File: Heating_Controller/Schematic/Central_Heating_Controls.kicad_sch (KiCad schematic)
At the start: 22 parts, among them J1 Mains In, J2 Output to Zone Valves, J3 Logic Control Input, J4 Thermostat Input, J5 Boiler Demand, J6 Valve(s) Open, K1 Zone 1, K2 Zone 2, K3 Zone 3, K4 Zone 4, K5 Boiler Demand, SW1 Zone 1 Mode, SW2 Zone 2 Mode, SW3 Zone 3 Mode, SW4 Zone 4 (HW) Mode, SW5 SW_SPST, SW6 Cylinder Stat

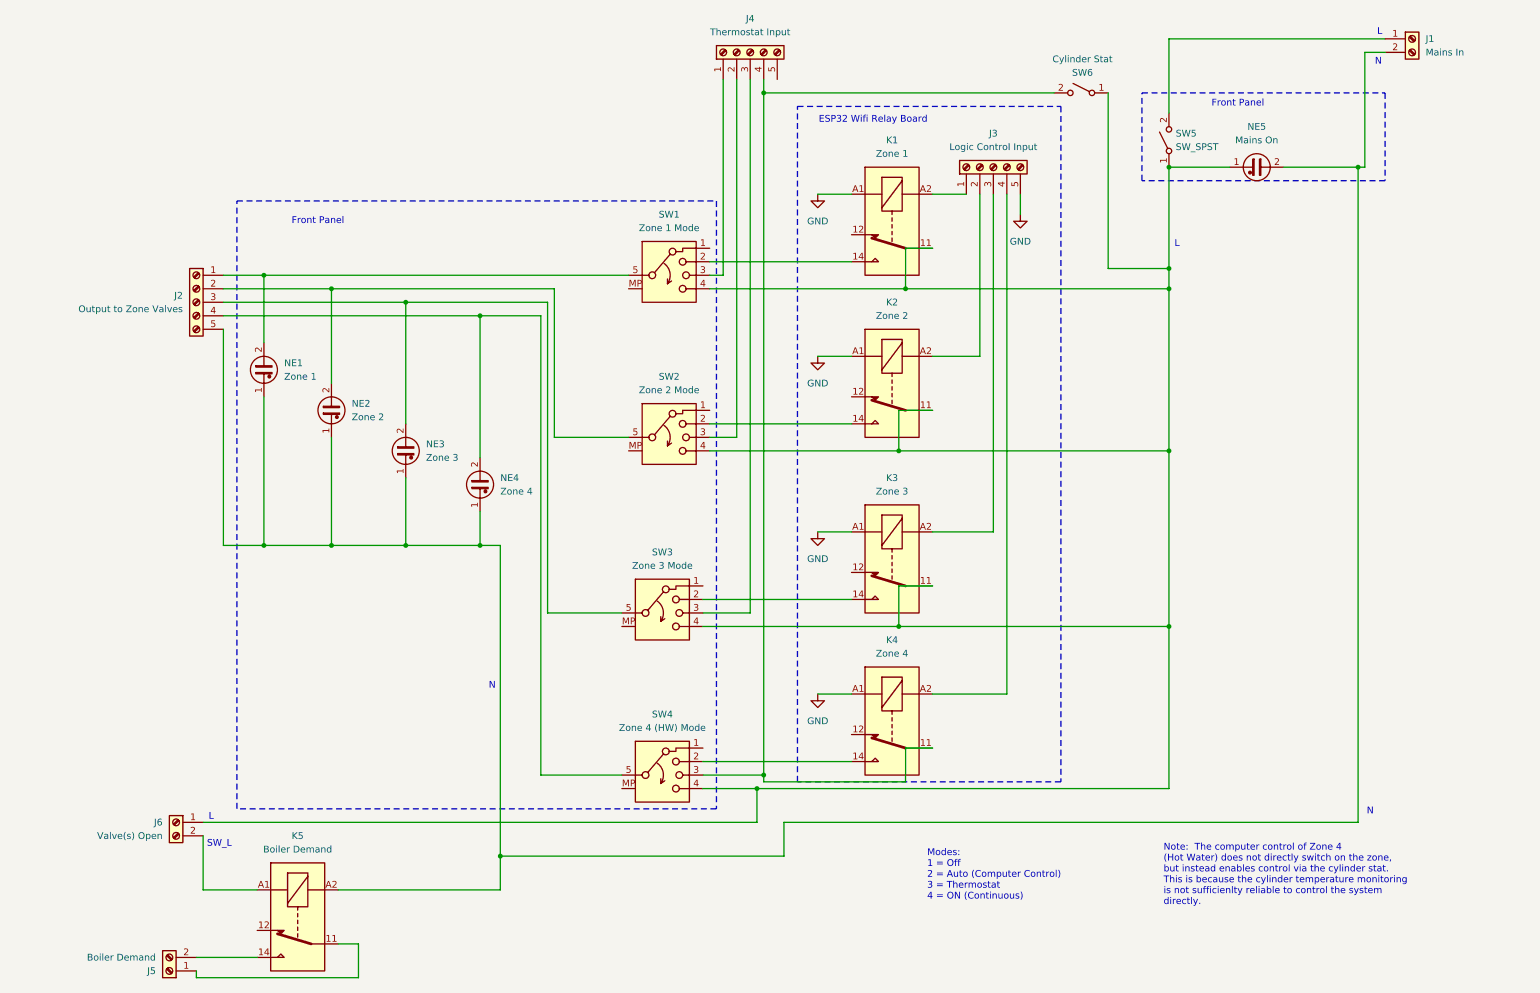
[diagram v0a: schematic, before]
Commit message: Re-ordered components on schematic to make it simpler to read
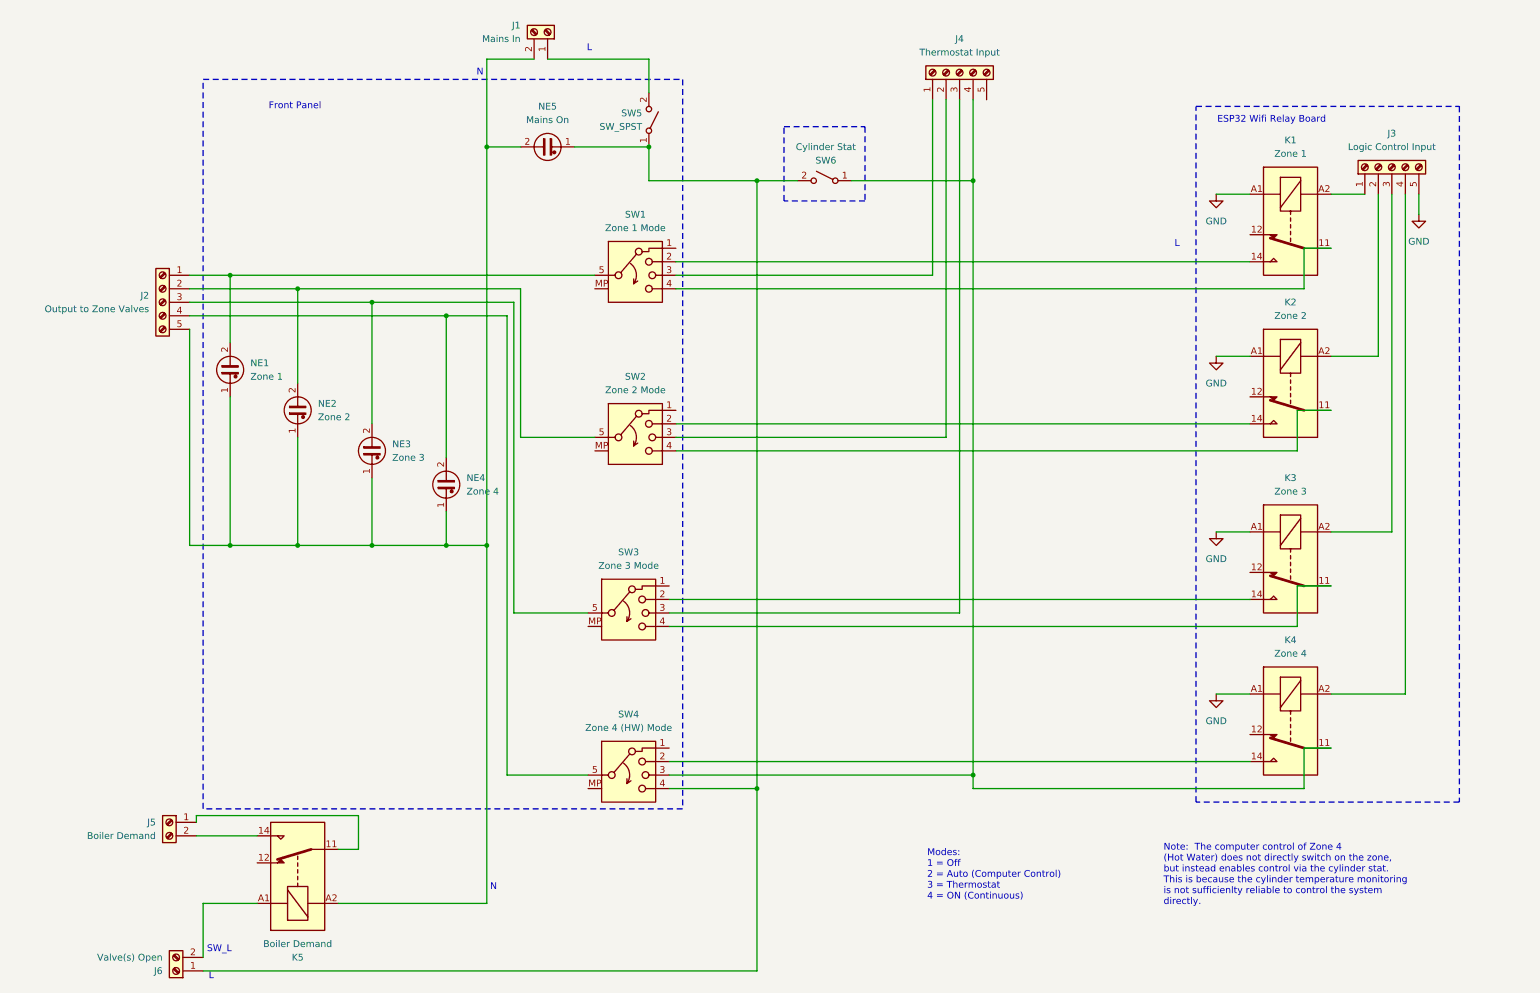
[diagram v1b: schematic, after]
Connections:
- net at J4.4 (Pin_4), K4.11, SW4.3: now also SW6.1 (A); no longer SW6.2 (B)
- new net: K2.11, SW2.4
- new net: K3.11, SW3.4
- new net: J6.1 (Pin_1), NE5.1, SW4.4, SW5.1 (A), SW6.2 (B)
- new net: K1.11, SW1.4
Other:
- moved on the sheet: J1, J2, J3, J4, J5, J6, K1, K2, K3, K4, K5, NE1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

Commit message: Added extra sheets to schematic for thermostat relay panel and valves junction box.
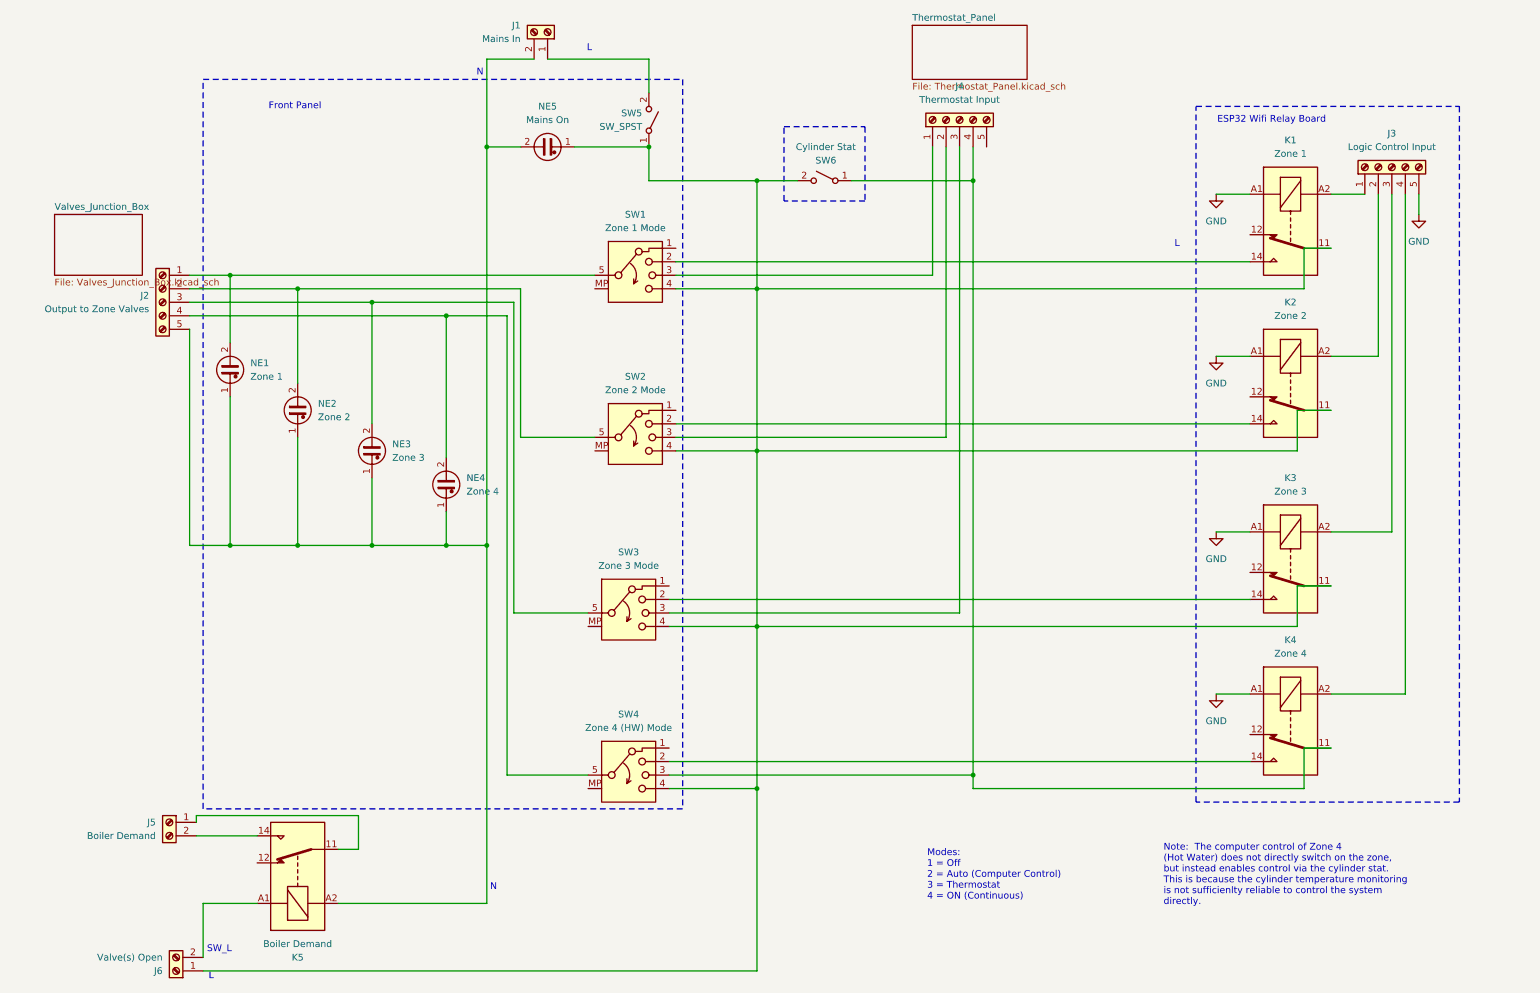
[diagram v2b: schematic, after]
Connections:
- net at K2.11, SW2.4: now also J6.1 (Pin_1), K1.11, K3.11, NE5.1, SW1.4, SW3.4, SW4.4, SW5.1 (A), SW6.2 (B)
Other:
- added sheet Thermostat_Panel (Thermostat_Panel.kicad_sch)
- added sheet Valves_Junction_Box (Valves_Junction_Box.kicad_sch)
- moved on the sheet: J4
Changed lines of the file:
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@@
 	(title_block
 		(title "Boiler Control Panel 1")
-		(date "05/12/2024")
-		(rev "2")
+		(date "11/12/2024")
+		(rev "3")
 	)
 	(junction
@@
 	)
 	(junction
+		(at 148.59 127)
+		(diameter 0)
+		(color 0 0 0 0)
+	)
+	(junction
 		(at 148.59 43.18)
 		(diameter 0)
@@
 	)
 	(junction
+		(at 148.59 63.5)
+		(diameter 0)
+		(color 0 0 0 0)
+	)
+	(junction
 		(at 76.2 111.76)
 		(diameter 0)
 		(color 0 0 0 0)
 	)
+	(junction
+		(at 148.59 93.98)
+		(diameter 0)
+		(color 0 0 0 0)
+	)
 	(wire
 		(pts
@@
 	(wire
 		(pts
-			(xy 133.35 63.5) (xy 251.46 63.5)
+			(xy 133.35 63.5) (xy 148.59 63.5)
 		)
 		(stroke
@@
 	(wire
 		(pts
-			(xy 148.59 157.48) (xy 148.59 43.18)
+			(xy 148.59 157.48) (xy 148.59 127)
 		)
 		(stroke
@@
 	(wire
 		(pts
-			(xy 132.08 127) (xy 250.19 127)
+			(xy 132.08 127) (xy 148.59 127)
 		)
 		(stroke
@@
 	(wire
 		(pts
-			(xy 189.23 27.94) (xy 189.23 43.18)
-		)
-		(stroke
-			(width 0)
-			(type default)
-		)
-	)
-	(wire
-		(pts
-			(xy 186.69 27.94) (xy 186.69 124.46)
+			(xy 189.23 36.83) (xy 189.23 43.18)
+		)
+		(stroke
+			(width 0)
+			(type default)
+		)
+	)
+	(wire
+		(pts
+			(xy 186.69 36.83) (xy 186.69 124.46)
 		)
 		(stroke
@@
 	(wire
 		(pts
+			(xy 148.59 127) (xy 250.19 127)
+		)
+		(stroke
+			(width 0)
+			(type default)
+		)
+	)
+	(wire
+		(pts
 			(xy 90.17 105.41) (xy 90.17 111.76)
 		)
@@
 	(wire
 		(pts
+			(xy 148.59 93.98) (xy 148.59 63.5)
+		)
+		(stroke
+			(width 0)
+			(type default)
+		)
+	)
+	(wire
+		(pts
 			(xy 97.79 179.07) (xy 69.85 179.07)
 		)
@@
 	(wire
 		(pts
+			(xy 148.59 127) (xy 148.59 93.98)
+		)
+		(stroke
+			(width 0)
+			(type default)
+		)
+	)
+	(wire
+		(pts
+			(xy 148.59 63.5) (xy 148.59 43.18)
+		)
+		(stroke
+			(width 0)
+			(type default)
+		)
+	)
+	(wire
+		(pts
 			(xy 128.27 43.18) (xy 128.27 36.83)
 		)
@@
 	(wire
 		(pts
-			(xy 184.15 27.94) (xy 184.15 91.44)
+			(xy 184.15 36.83) (xy 184.15 91.44)
 		)
 		(stroke
@@
 	(wire
 		(pts
-			(xy 181.61 27.94) (xy 181.61 60.96)
+			(xy 148.59 93.98) (xy 250.19 93.98)
+		)
+		(stroke
+			(width 0)
+			(type default)
+		)
+	)
+	(wire
+		(pts
+			(xy 181.61 36.83) (xy 181.61 60.96)
 		)
 		(stroke
@@
 	(wire
 		(pts
-			(xy 133.35 93.98) (xy 250.19 93.98)
+			(xy 148.59 63.5) (xy 251.46 63.5)
+		)
+		(stroke
+			(width 0)
+			(type default)
+		)
+	)
+	(wire
+		(pts
+			(xy 133.35 93.98) (xy 148.59 93.98)
 		)
 		(stroke
@@
 	(symbol
 		(lib_id "Connector:Screw_Terminal_01x05")
-		(at 186.69 22.86 90)
+		(at 186.69 31.75 90)
 		(unit 1)
 		(exclude_from_sim no)
@@
 		(fields_autoplaced yes)
 		(property "Reference" "J4"
-			(at 186.69 16.51 90)
+			(at 186.69 25.4 90)
 			(effects
 				(font
@@
 		)
 		(property "Value" "Thermostat Input"
-			(at 186.69 19.05 90)
+			(at 186.69 27.94 90)
 			(effects
 				(font
@@
 		)
 		(property "Footprint" ""
-			(at 186.69 22.86 0)
+			(at 186.69 31.75 0)
 			(effects
 				(font
@@
 		)
 		(property "Datasheet" "~"
-			(at 186.69 22.86 0)
+			(at 186.69 31.75 0)
 			(effects
 				(font
@@
 		)
 		(property "Description" "Generic screw terminal, single row, 01x05, script generated (kicad-library-utils/schlib/autogen/connector/)"
-			(at 186.69 22.86 0)
+			(at 186.69 31.75 0)
 			(effects
 				(font
@@
 				)
 			)
+		)
+	)
+	(sheet
+		(at 16.51 49.53)
+		(size 16.51 11.43)
+		(fields_autoplaced yes)
+		(stroke
+			(width 0.1524)
+			(type solid)
+		)
+		(fill
+			(color 0 0 0 0.0000)
+		)
+		(property "Sheetname" "Valves_Junction_Box"
+			(at 16.51 48.8184 0)
+			(effects
+				(font
+					(size 1.27 1.27)
+				)
+				(justify left bottom)
+			)
+		)
+		(property "Sheetfile" "Valves_Junction_Box.kicad_sch"
+			(at 16.51 61.5446 0)
+			(effects
+				(font
+					(size 1.27 1.27)
+				)
+				(justify left top)
+			)
+		)
+		(instances
+			(project "Central_Heating_Controls"
+				(path "/cd955688-bdae-4275-b855-3d8eea9a4e1c"
+					(page "3")
+				)
+			)
+		)
+	)
+	(sheet
+		(at 177.8 13.97)
+		(size 21.59 10.16)
+		(fields_autoplaced yes)
+		(stroke
+			(width 0.1524)
+			(type solid)
+		)
+		(fill
+			(color 0 0 0 0.0000)
+		)
+		(property "Sheetname" "Thermostat_Panel"
+			(at 177.8 13.2584 0)
+			(effects
+				(font
+					(size 1.27 1.27)
+				)
+				(justify left bottom)
+			)
+		)
+		(property "Sheetfile" "Thermostat_Panel.kicad_sch"
+			(at 177.8 24.7146 0)
+			(effects
+				(font
+					(size 1.27 1.27)
+				)
+				(justify left top)
+			)
+		)
+		(instances
+			(project "Central_Heating_Controls"
+				(path "/cd955688-bdae-4275-b855-3d8eea9a4e1c"
+					(page "2")
+				)
+			)

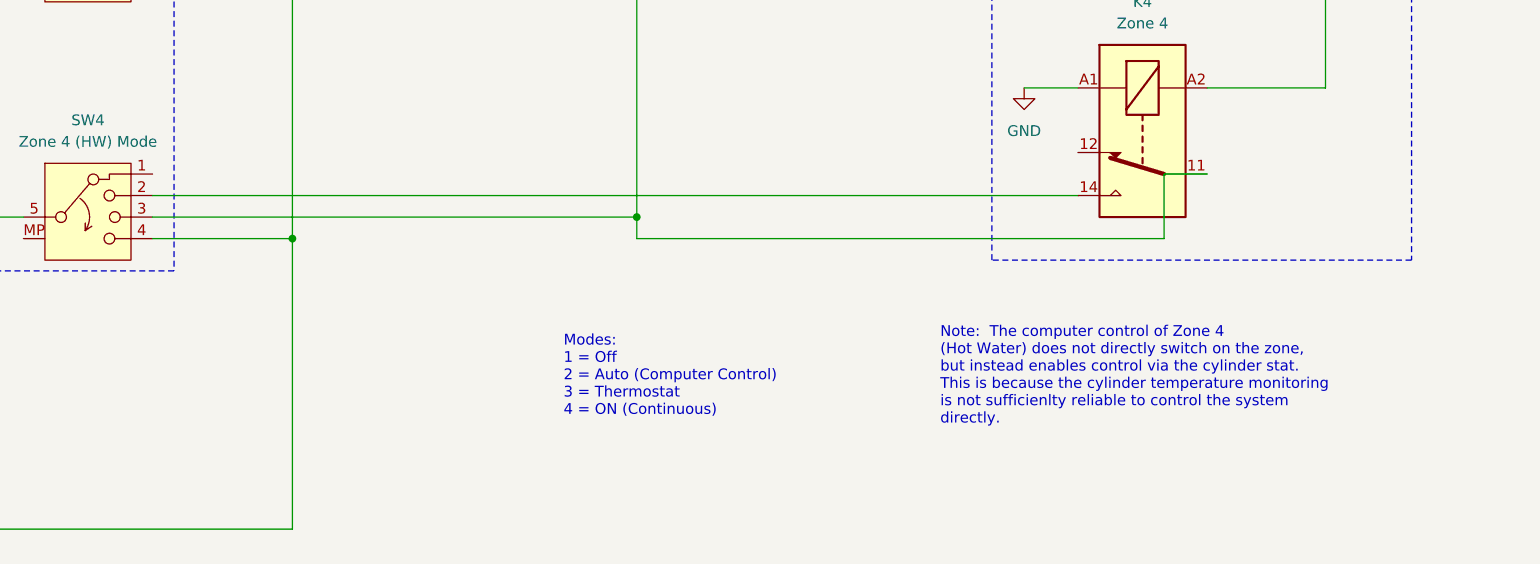
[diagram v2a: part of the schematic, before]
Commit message: Updated schematic to show DHW relay normally de-energised
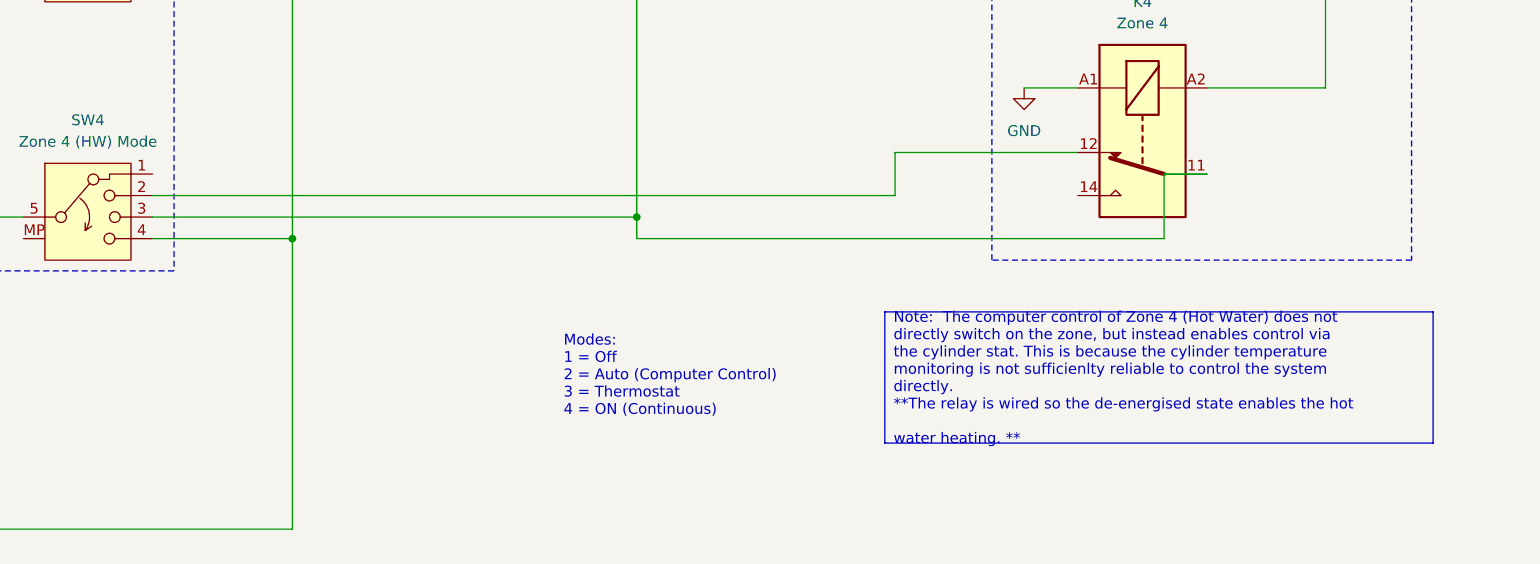
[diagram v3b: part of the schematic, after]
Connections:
- net at SW4.2: now also K4.12; no longer K4.14
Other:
- note removed: "Note: The computer control of Zone 4 (Hot Water) does not directly switch on the zone, but instead enables control via the cylinder stat. This is because the cylinder temperature monitoring is not sufficienlty reliable to control the system directly."
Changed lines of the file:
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@@
 	(title_block
 		(title "Boiler Control Panel 1")
-		(date "11/12/2024")
-		(rev "3")
+		(date "2024-12-19")
+		(rev "4")
 	)
 	(junction
@@
 	(wire
 		(pts
+			(xy 219.71 147.32) (xy 241.3 147.32)
+		)
+		(stroke
+			(width 0)
+			(type default)
+		)
+	)
+	(wire
+		(pts
 			(xy 62.23 63.5) (xy 104.14 63.5)
 		)
@@
 	(wire
 		(pts
+			(xy 219.71 152.4) (xy 219.71 147.32)
+		)
+		(stroke
+			(width 0)
+			(type default)
+		)
+	)
+	(wire
+		(pts
 			(xy 49.53 111.76) (xy 62.23 111.76)
 		)
@@
 	(wire
 		(pts
-			(xy 132.08 152.4) (xy 241.3 152.4)
-		)
-		(stroke
-			(width 0)
-			(type default)
-		)
-	)
-	(wire
-		(pts
 			(xy 132.08 157.48) (xy 148.59 157.48)
 		)
@@
 		(pts
 			(xy 133.35 58.42) (xy 241.3 58.42)
+		)
+		(stroke
+			(width 0)
+			(type default)
+		)
+	)
+	(wire
+		(pts
+			(xy 132.08 152.4) (xy 219.71 152.4)
 		)
 		(stroke
@@
 			(type color)
 			(color 224 224 224 1)
+		)
+	)
+	(text_box "Note:  The computer control of Zone 4 (Hot Water) does not \ndirectly switch on the zone, but instead enables control via \nthe cylinder stat. This is because the cylinder temperature \nmonitoring is not sufficienlty reliable to control the system \ndirectly.  \n**The relay is wired so the de-energised state enables the hot \n  water heating. **"
+		(exclude_from_sim no)
+		(at 218.5035 166.1297 0)
+		(size 64.7065 15.4803)
+		(stroke
+			(width 0)
+			(type default)
+		)
+		(fill
+			(type none)
+		)
+		(effects
+			(font
+				(size 1.27 1.27)
+				(thickness 0.1588)
+			)
+			(justify left)
 		)
 	)
@@
 		)
 	)
-	(text "Note:  The computer control of Zone 4 \n(Hot Water) does not directly switch on the zone, \nbut instead enables control via the cylinder stat.\nThis is because the cylinder temperature monitoring\nis not sufficienlty reliable to control the system \ndirectly."
-		(exclude_from_sim no)
-		(at 225.044 173.736 0)
-		(effects
-			(font
-				(size 1.27 1.27)
-			)
-			(justify left)
-		)
-	)
